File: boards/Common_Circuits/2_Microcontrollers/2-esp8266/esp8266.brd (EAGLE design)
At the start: 31 x 37 mm, 11 parts, among them X1 ESP-12

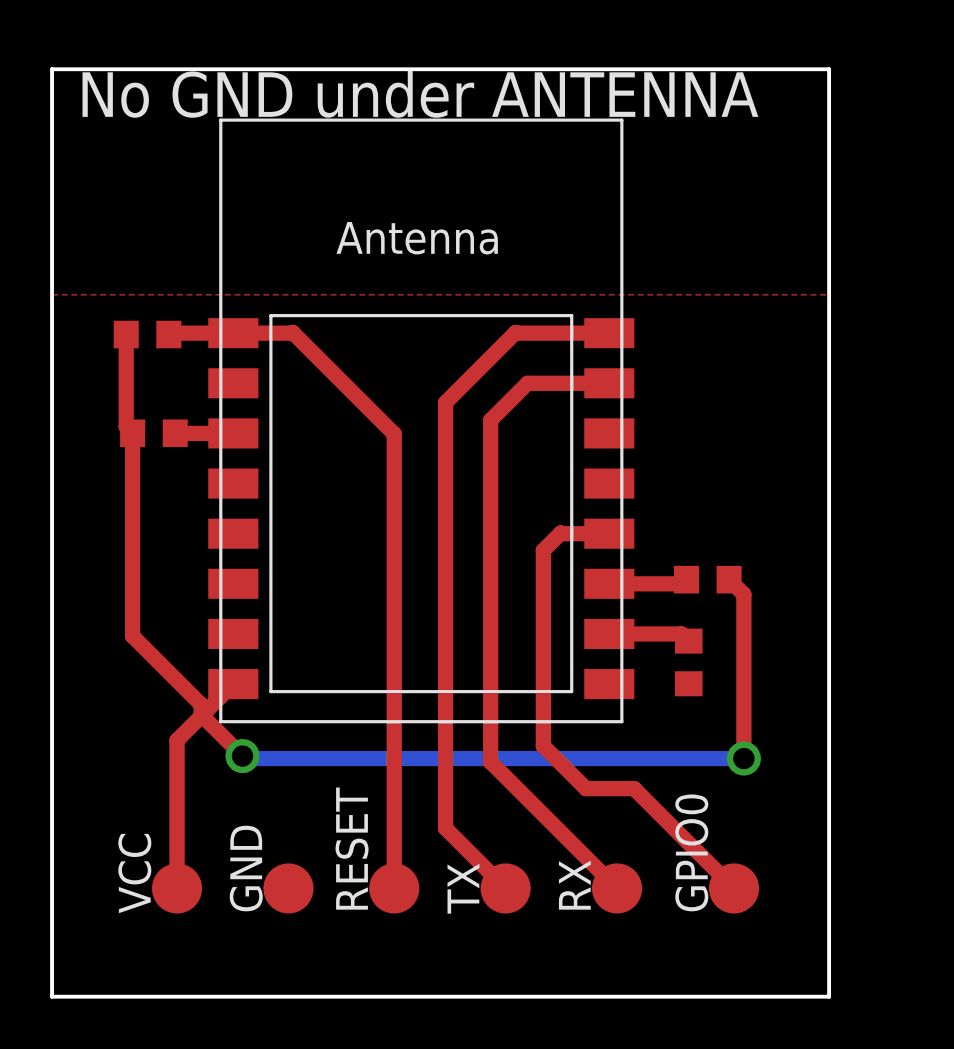
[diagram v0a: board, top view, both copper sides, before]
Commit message: adds ESP8266 board to common circuits
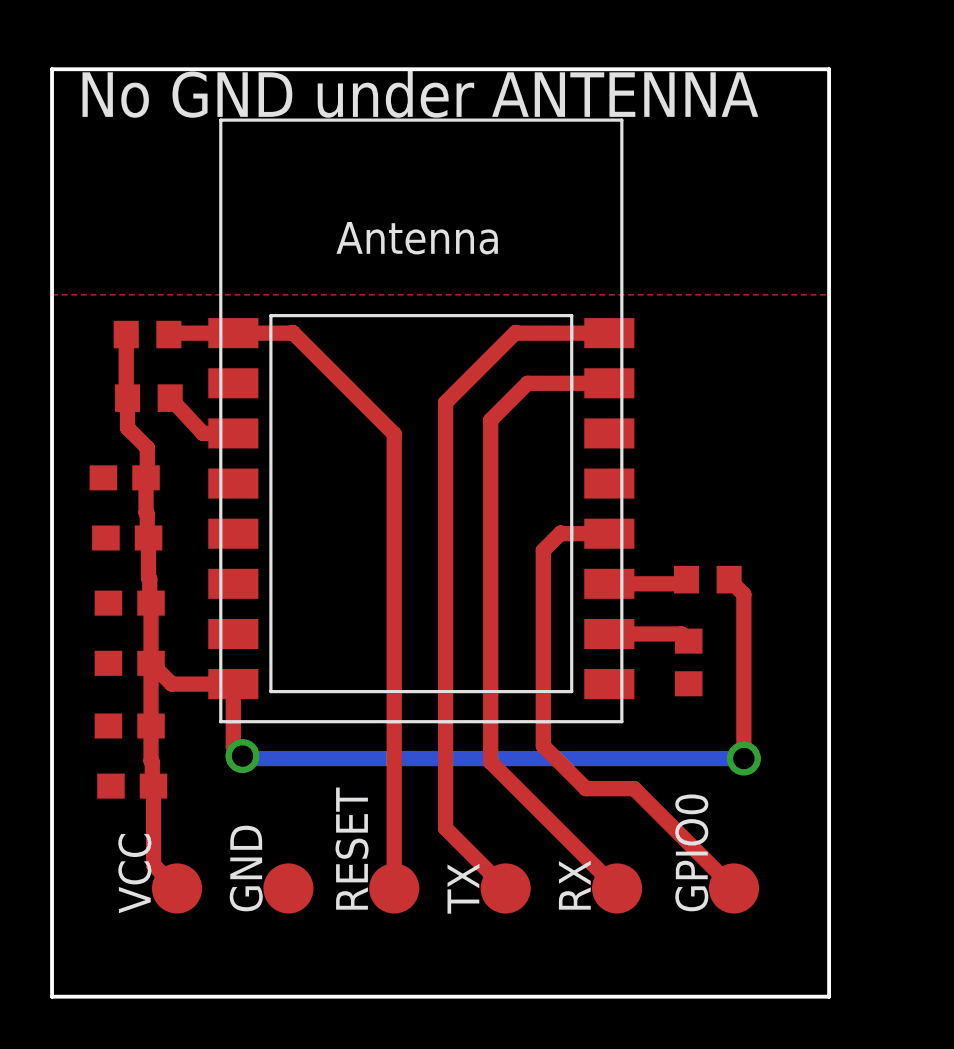
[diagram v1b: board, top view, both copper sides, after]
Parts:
- added C1, C6: 0.1uF, SparkFun-Capacitors:0603
- added C2, C3, C4, C5: 4.7uF, SparkFun-Capacitors:0603
- moved R8 1.41 mm to (3.86, 23.9)
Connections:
- net GND: now also C1.2, C2.2, C3.2, C4.2, C5.2, C6.2
- net VCC: now also C1.1, C2.1, C3.1, C4.1, C5.1, C6.1
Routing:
- net VCC: track 55.6 -> 57.0 mm
- net CH_PD: track 2.32 -> 3.13 mm
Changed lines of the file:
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@@
 <element name="R3" library="rcl" library_urn="urn:adsk.eagle:library:334" package="R0603" package3d_urn="urn:adsk.eagle:package:23555/2" value="10k" x="3.81" y="26.416" smashed="yes" rot="R180">
 <attribute name="SPICEPREFIX" value="R" x="3.81" y="26.416" size="1.778" layer="27" rot="R180" display="off"/>
-<attribute name="VALUE" x="2.455" y="27.579" size="1.27" layer="27"/>
+<attribute name="VALUE" x="1.621" y="25.955" size="1.27" layer="27" rot="R90"/>
 </element>
 <element name="R5" library="rcl" library_urn="urn:adsk.eagle:library:334" package="R0603" package3d_urn="urn:adsk.eagle:package:23555/2" value="10k" x="26.162" y="16.637" smashed="yes">
@@
 <attribute name="VALUE" x="24.827" y="17.932" size="1.27" layer="27"/>
 </element>
-<element name="R8" library="rcl" library_urn="urn:adsk.eagle:library:334" package="R0603" package3d_urn="urn:adsk.eagle:package:23555/2" value="10k" x="4.064" y="22.479" smashed="yes" rot="R180">
-<attribute name="SPICEPREFIX" value="R" x="4.064" y="22.479" size="1.778" layer="27" rot="R180" display="off"/>
-<attribute name="VALUE" x="3.201" y="23.516" size="1.27" layer="27"/>
+<element name="R8" library="rcl" library_urn="urn:adsk.eagle:library:334" package="R0603" package3d_urn="urn:adsk.eagle:package:23555/2" value="10k" x="3.864" y="23.879" smashed="yes" rot="R180">
+<attribute name="SPICEPREFIX" value="R" x="3.864" y="23.879" size="1.778" layer="27" rot="R180" display="off"/>
+<attribute name="VALUE" x="1.684" y="22.701" size="1.27" layer="27" rot="R90"/>
 </element>
 <element name="R9" library="rcl" library_urn="urn:adsk.eagle:library:334" package="R0603" package3d_urn="urn:adsk.eagle:package:23555/2" value="10k" x="25.4" y="13.335" smashed="yes" rot="R90">
@@
 <attribute name="VALUE" x="10.448" y="3.556" size="0.0254" layer="27" rot="R90"/>
 </element>
+<element name="C1" library="SparkFun-Capacitors" package="0603" value="0.1uF" x="3.1" y="10.8" smashed="yes" rot="R180">
+<attribute name="PROD_ID" value="CAP-08604" x="3.1" y="10.8" size="1.778" layer="27" rot="R180" display="off"/>
+<attribute name="VALUE" x="3.1" y="11.562" size="0.6096" layer="27" font="vector" ratio="20" rot="R180" align="top-center"/>
+</element>
+<element name="C2" library="SparkFun-Capacitors" package="0603" value="4.7uF" x="2.9" y="20.7" smashed="yes" rot="R180">
+<attribute name="PROD_ID" value="CAP-08280" x="2.9" y="20.7" size="1.778" layer="27" rot="R180" display="off"/>
+<attribute name="VALUE" x="2.9" y="21.462" size="0.6096" layer="27" font="vector" ratio="20" rot="R180" align="top-center"/>
+</element>
+<element name="C3" library="SparkFun-Capacitors" package="0603" value="4.7uF" x="3" y="18.3" smashed="yes" rot="R180">
+<attribute name="PROD_ID" value="CAP-08280" x="3" y="18.3" size="1.778" layer="27" rot="R180" display="off"/>
+<attribute name="VALUE" x="3" y="19.062" size="0.6096" layer="27" font="vector" ratio="20" rot="R180" align="top-center"/>
+</element>
+<element name="C4" library="SparkFun-Capacitors" package="0603" value="4.7uF" x="3.1" y="15.7" smashed="yes" rot="R180">
+<attribute name="PROD_ID" value="CAP-08280" x="3.1" y="15.7" size="1.778" layer="27" rot="R180" display="off"/>
+<attribute name="VALUE" x="3.1" y="16.462" size="0.6096" layer="27" font="vector" ratio="20" rot="R180" align="top-center"/>
+</element>
+<element name="C5" library="SparkFun-Capacitors" package="0603" value="4.7uF" x="3.1" y="13.3" smashed="yes" rot="R180">
+<attribute name="PROD_ID" value="CAP-08280" x="3.1" y="13.3" size="1.778" layer="27" rot="R180" display="off"/>
+<attribute name="VALUE" x="3.1" y="14.062" size="0.6096" layer="27" font="vector" ratio="20" rot="R180" align="top-center"/>
+</element>
+<element name="C6" library="SparkFun-Capacitors" package="0603" value="0.1uF" x="3.2" y="8.4" smashed="yes" rot="R180">
+<attribute name="PROD_ID" value="CAP-08604" x="3.2" y="8.4" size="1.778" layer="27" rot="R180" display="off"/>
+<attribute name="VALUE" x="3.2" y="9.162" size="0.6096" layer="27" font="vector" ratio="20" rot="R180" align="top-center"/>
+</element>
 </elements>
 <signals>
@@
 <contactref element="R9" pad="1"/>
 <contactref element="GND" pad="TP"/>
-<polygon width="0.6096" layer="1">
+<polygon width="0.4064" layer="1">
 <vertex x="0" y="28"/>
 <vertex x="31" y="28"/>
@@
 <vertex x="0" y="0"/>
 </polygon>
+<contactref element="C3" pad="2"/>
+<contactref element="C2" pad="2"/>
+<contactref element="C4" pad="2"/>
+<contactref element="C5" pad="2"/>
+<contactref element="C1" pad="2"/>
+<contactref element="C6" pad="2"/>
 </signal>
 <signal name="RESET">
@@
 <contactref element="X1" pad="3"/>
 <contactref element="R8" pad="1"/>
-<wire x1="7.232" y1="22.471" x2="4.922" y2="22.471" width="0.6096" layer="1"/>
-<wire x1="4.922" y1="22.471" x2="4.914" y2="22.479" width="0.6096" layer="1"/>
+<wire x1="7.232" y1="22.471" x2="6.022" y2="22.471" width="0.6096" layer="1"/>
+<wire x1="6.022" y1="22.471" x2="4.714" y2="23.879" width="0.6096" layer="1"/>
 </signal>
 <signal name="GPIO15">
@@
 <contactref element="R5" pad="2"/>
 <contactref element="VCC" pad="TP"/>
-<wire x1="4.987" y1="4.318" x2="4.987" y2="10.226" width="0.6096" layer="1"/>
-<wire x1="4.987" y1="10.226" x2="6.1805" y2="11.4195" width="0.6096" layer="1"/>
-<wire x1="6.1805" y1="11.4195" x2="7.232" y2="12.471" width="0.6096" layer="1"/>
-<wire x1="2.96" y1="26.416" x2="2.96" y2="22.733" width="0.6096" layer="1"/>
-<wire x1="2.96" y1="22.733" x2="3.214" y2="22.479" width="0.6096" layer="1"/>
-<wire x1="3.214" y1="22.479" x2="3.214" y2="14.386" width="0.6096" layer="1"/>
-<wire x1="3.214" y1="14.386" x2="5.95" y2="11.65" width="0.6096" layer="1"/>
-<wire x1="5.95" y1="11.65" x2="6.1805" y2="11.4195" width="0.6096" layer="1"/>
 <wire x1="27.012" y1="16.637" x2="27.6" y2="16.049" width="0.6096" layer="1"/>
 <wire x1="27.6" y1="16.049" x2="27.6" y2="9.5" width="0.6096" layer="1"/>
@@
 <wire x1="7.7" y1="9.5" x2="7.6" y2="9.6" width="0.6096" layer="16"/>
 <via x="7.6" y="9.6" extent="1-16" drill="0.85"/>
-<wire x1="7.6" y1="9.6" x2="5.95" y2="11.25" width="0.6096" layer="1"/>
-<wire x1="5.95" y1="11.25" x2="5.95" y2="11.65" width="0.6096" layer="1"/>
+<contactref element="C3" pad="1"/>
+<contactref element="C2" pad="1"/>
+<contactref element="C4" pad="1"/>
+<contactref element="C5" pad="1"/>
+<contactref element="C1" pad="1"/>
+<contactref element="C6" pad="1"/>
+<wire x1="7.6" y1="9.6" x2="7.232" y2="9.968" width="0.6096" layer="1"/>
+<wire x1="7.232" y1="9.968" x2="7.232" y2="12.471" width="0.6096" layer="1"/>
+<wire x1="2.96" y1="26.416" x2="2.96" y2="23.933" width="0.6096" layer="1"/>
+<wire x1="2.96" y1="23.933" x2="3.014" y2="23.879" width="0.6096" layer="1"/>
+<wire x1="3.014" y1="23.879" x2="3.014" y2="22.686" width="0.6096" layer="1"/>
+<wire x1="3.014" y1="22.686" x2="3.8" y2="21.9" width="0.6096" layer="1"/>
+<wire x1="3.8" y1="21.9" x2="3.8" y2="20.75" width="0.6096" layer="1"/>
+<wire x1="3.8" y1="20.75" x2="3.75" y2="20.7" width="0.6096" layer="1"/>
+<wire x1="3.75" y1="20.7" x2="3.75" y2="19.3039375" width="0.6096" layer="1"/>
+<wire x1="3.75" y1="19.3039375" x2="3.7988" y2="19.2551375" width="0.6096" layer="1"/>
+<wire x1="3.7988" y1="19.2551375" x2="3.7988" y2="18.3512" width="0.6096" layer="1"/>
+<wire x1="3.7988" y1="18.3512" x2="3.85" y2="18.3" width="0.6096" layer="1"/>
+<wire x1="3.85" y1="18.3" x2="3.85" y2="16.7039375" width="0.6096" layer="1"/>
+<wire x1="3.85" y1="16.7039375" x2="3.8988" y2="16.6551375" width="0.6096" layer="1"/>
+<wire x1="3.8988" y1="16.6551375" x2="3.8988" y2="15.7512" width="0.6096" layer="1"/>
+<wire x1="3.8988" y1="15.7512" x2="3.95" y2="15.7" width="0.6096" layer="1"/>
+<wire x1="3.95" y1="15.7" x2="3.95" y2="13.3" width="0.6096" layer="1"/>
+<wire x1="7.232" y1="12.471" x2="4.779" y2="12.471" width="0.6096" layer="1"/>
+<wire x1="4.779" y1="12.471" x2="3.95" y2="13.3" width="0.6096" layer="1"/>
+<wire x1="3.95" y1="13.3" x2="3.95" y2="10.8" width="0.6096" layer="1"/>
+<wire x1="3.95" y1="10.8" x2="3.95" y2="9.4039375" width="0.6096" layer="1"/>
+<wire x1="3.95" y1="9.4039375" x2="3.9988" y2="9.3551375" width="0.6096" layer="1"/>
+<wire x1="3.9988" y1="9.3551375" x2="3.9988" y2="8.4512" width="0.6096" layer="1"/>
+<wire x1="3.9988" y1="8.4512" x2="4.05" y2="8.4" width="0.6096" layer="1"/>
+<wire x1="4.05" y1="8.4" x2="4.05" y2="5.255" width="0.6096" layer="1"/>
+<wire x1="4.05" y1="5.255" x2="4.987" y2="4.318" width="0.6096" layer="1"/>
 </signal>
 </signals>

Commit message: adds REgulators example to common circuits
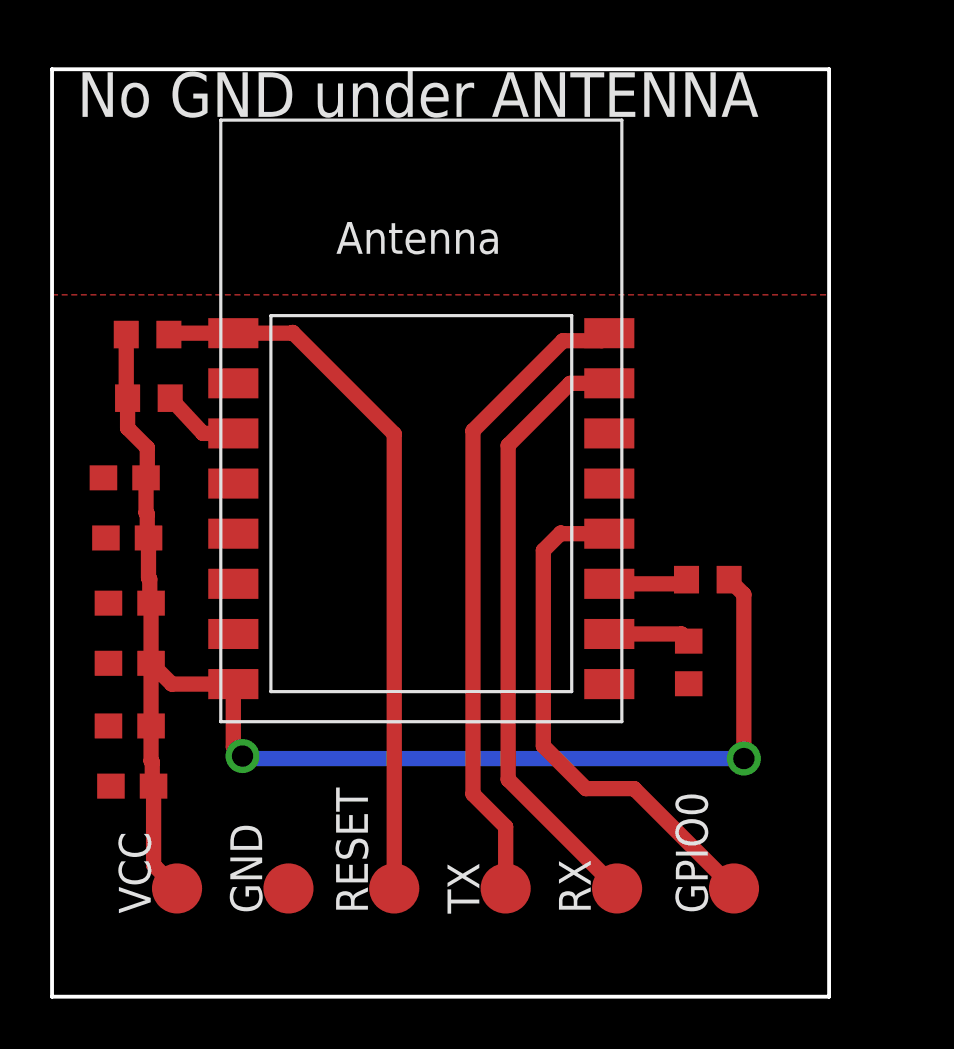
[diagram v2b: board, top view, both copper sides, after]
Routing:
- net TXD: track 28.1 -> 25.9 mm
- net RXD: track 26.1 -> 24.5 mm
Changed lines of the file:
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@@
 <contactref element="X1" pad="15"/>
 <contactref element="RX" pad="TP"/>
-<wire x1="22.232" y1="24.471" x2="18.971" y2="24.471" width="0.6096" layer="1"/>
-<wire x1="18.971" y1="24.471" x2="17.5" y2="23" width="0.6096" layer="1"/>
-<wire x1="17.5" y1="23" x2="17.5" y2="9.36" width="0.6096" layer="1"/>
-<wire x1="17.5" y1="9.36" x2="22.542" y2="4.318" width="0.6096" layer="1"/>
+<wire x1="22.542" y1="4.318" x2="18.19639375" y2="8.66360625" width="0.6096" layer="1"/>
+<wire x1="20.671" y1="24.471" x2="22.232" y2="24.471" width="0.6096" layer="1"/>
+<wire x1="18.19639375" y1="8.66360625" x2="18.19639375" y2="21.99639375" width="0.6096" layer="1"/>
+<wire x1="18.19639375" y1="21.99639375" x2="20.671" y2="24.471" width="0.6096" layer="1"/>
 </signal>
 <signal name="TXD">
 <contactref element="X1" pad="16"/>
 <contactref element="TX" pad="TP"/>
-<wire x1="18.097" y1="4.318" x2="15.7" y2="6.715" width="0.6096" layer="1"/>
-<wire x1="15.7" y1="23.7" x2="18.5" y2="26.5" width="0.6096" layer="1"/>
-<wire x1="18.5" y1="26.5" x2="18.529" y2="26.471" width="0.6096" layer="1"/>
-<wire x1="18.529" y1="26.471" x2="22.232" y2="26.471" width="0.6096" layer="1"/>
-<wire x1="15.7" y1="6.715" x2="15.7" y2="23.7" width="0.6096" layer="1"/>
+<wire x1="21.9308" y1="26.1698" x2="22.232" y2="26.471" width="0.6096" layer="1"/>
+<wire x1="20.3848" y1="26.1698" x2="21.9308" y2="26.1698" width="0.6096" layer="1"/>
+<wire x1="18.097" y1="4.318" x2="18.097" y2="6.778" width="0.6096" layer="1"/>
+<wire x1="18.097" y1="6.778" x2="16.7927875" y2="8.0822125" width="0.6096" layer="1"/>
+<wire x1="16.7927875" y1="8.0822125" x2="16.7927875" y2="22.5777875" width="0.6096" layer="1"/>
+<wire x1="16.7927875" y1="22.5777875" x2="20.3848" y2="26.1698" width="0.6096" layer="1"/>
 </signal>
 <signal name="VCC">
